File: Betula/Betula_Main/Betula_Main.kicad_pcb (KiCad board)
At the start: 2 copper layers, 39.4 x 110.1 mm, 172 parts, among them J1 Conn_02x15_Top_Bottom, J2 Conn_02x02_Top_Bottom, J3 Conn_02x15_Top_Bottom, J4 Conn_01x03_Male, J5 Conn_01x03_Male, J6 Conn_02x05_Odd_Even, Q1 FDS4435BZ, Q2 DMN3030LSS, U1 PCM1803A, U10 V1402, U11 74HCT125, U12 TLV9354, U13 TLV9354, U14 TLV9352, U15 TLV9354, U16 TLV9354, U2 PCM1803A, U3 PCM1803A, U4 PCM1803A, U5 LDK320A, U6 TL062, U7 PCM1681TPWPQ1, U8 74HC4050, U9 V1401

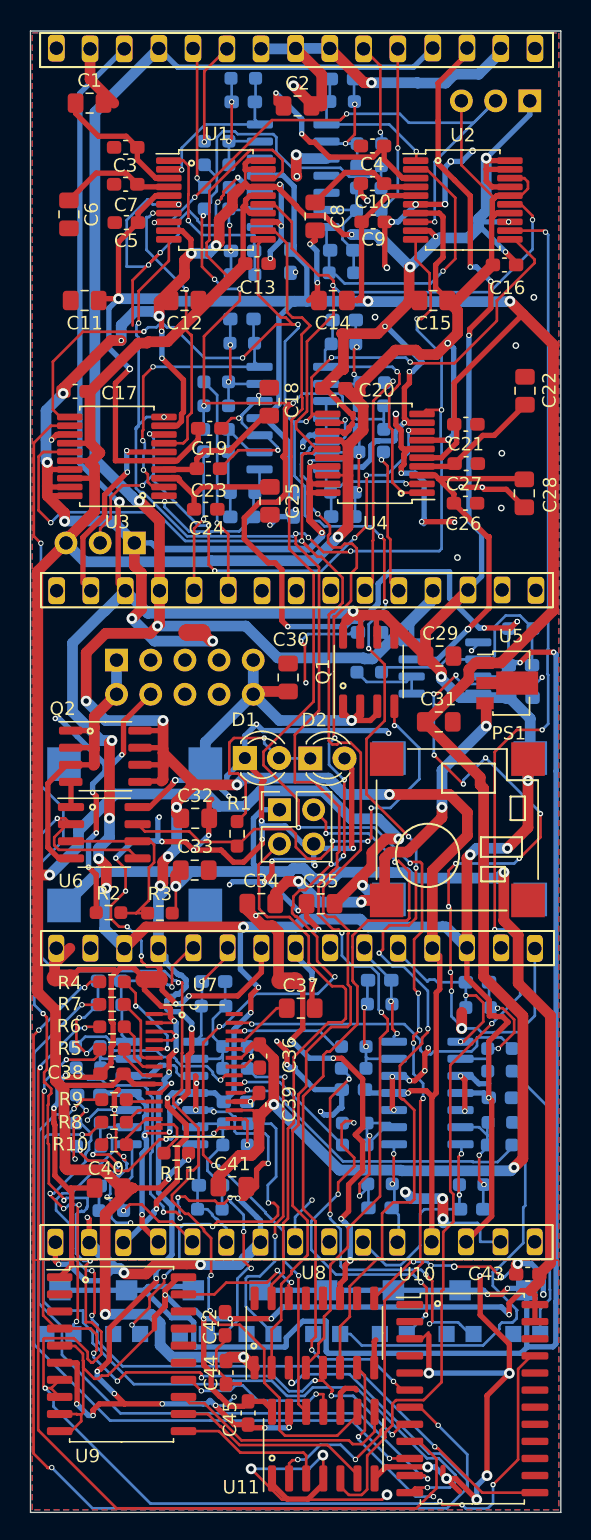
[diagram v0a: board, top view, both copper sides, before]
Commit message: Added Betula v1.5.1:  Improved noise floor, 4-layer main PCB, better Panel
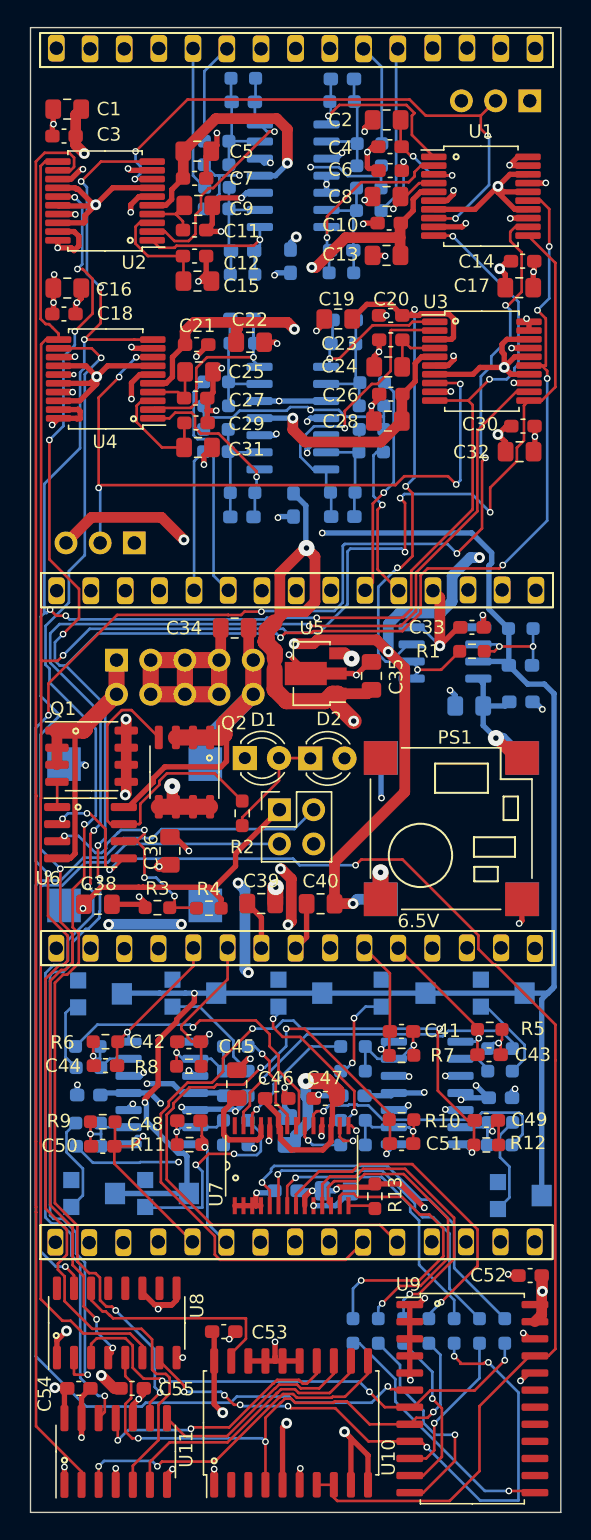
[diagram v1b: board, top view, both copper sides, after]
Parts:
- removed the C29 at (121.9, 78.6)
- removed NT1, NT2, NT3, NT4: NetTie_2, NetTie:NetTie-2_SMD_Pad2.0mm
- added C16: 10u, Capacitor_SMD:C_0805_2012Metric_Pad1.18x1.45mm_HandSolder, F.Cu at (94.2, 51.3)
- added C22: 10u, Capacitor_SMD:C_0805_2012Metric_Pad1.18x1.45mm_HandSolder, F.Cu at (107.8, 55.3)
- added C28: 10u, Capacitor_SMD:C_0805_2012Metric_Pad1.18x1.45mm_HandSolder, F.Cu at (118.0, 61.2)
- added C32: 10u, Capacitor_SMD:C_0805_2012Metric_Pad1.18x1.45mm_HandSolder, F.Cu at (127.8, 63.5)
- added C68: 10uF, Capacitor_SMD:C_0805_2012Metric_Pad1.18x1.45mm_HandSolder, B.Cu at (124.1, 82.3)
- C33: renamed from C56; moved to F.Cu
- C38: renamed from C33; value 10uF -> 22uF
- C39: renamed from C34; value 10uF -> 22uF
- C40: renamed from C35; value 10uF -> 22uF
- C41: renamed from C60; moved to F.Cu
- C42: renamed from C61; moved to F.Cu
- C43: renamed from C59; moved to F.Cu
- C44: renamed from C62; moved to F.Cu
- C48: renamed from C67; moved to F.Cu
- C49: renamed from C69; moved to F.Cu
- C50: renamed from C68; moved to F.Cu
- C51: renamed from C70; moved to F.Cu
- C73: renamed from C41; moved to B.Cu
- C74: renamed from C40; moved to B.Cu
- C75: renamed from C38; moved to B.Cu
- R1: renamed from R37; moved to F.Cu
- R10: renamed from R56; moved to F.Cu
- R11: renamed from R60; moved to F.Cu
- R12: renamed from R55; moved to F.Cu
- R5: renamed from R38; moved to F.Cu
- R55: renamed from R4; moved to B.Cu
- R56: renamed from R7; moved to B.Cu
- R57: renamed from R6; moved to B.Cu
- R58: renamed from R5; moved to B.Cu
- R59: renamed from R9; moved to B.Cu
- R6: renamed from R46; moved to F.Cu
- R60: renamed from R8; moved to B.Cu
- R61: renamed from R10; moved to B.Cu
- R7: renamed from R40; moved to F.Cu
- R8: renamed from R42; moved to F.Cu
- R9: renamed from R61; moved to F.Cu
- moved R55 39.0 mm to (126.7, 128.8), turned to 90 degrees
- moved R56 36.5 mm to (124.8, 128.8), turned to 90 degrees
- moved R57 34.0 mm to (123.0, 128.8), turned to 90 degrees
- moved R58 31.5 mm to (121.1, 128.8), turned to 90 degrees
- moved R59 27.5 mm to (119.2, 128.8), turned to 90 degrees
- moved R60 25.0 mm to (117.3, 128.8), turned to 90 degrees
- moved RV3 24.5 mm to (111.7, 103.7), turned to 0 degrees
- moved RV5 24.4 mm to (96.8, 103.7), turned to 0 degrees
- moved RV4 24.0 mm to (103.8, 103.7), turned to 0 degrees
- moved RV2 23.9 mm to (119.4, 103.7), turned to 0 degrees
- moved RV1 23.6 mm to (126.7, 103.7), turned to 0 degrees
- moved R61 22.5 mm to (115.4, 128.8), turned to 90 degrees
- moved C19 18.9 mm to (114.3, 53.6), turned to 180 degrees
- moved C3 17.2 mm to (94.0, 40.0), turned to 0 degrees
- moved C74 16.9 mm to (114.2, 118.4), turned to 0 degrees
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- renumbered C12 to C1, C9 to C10, C7 to C11, C3 to C12, C14 to C13, C16 to C14, C1 to C15, C15 to C17, C17 to C18, C28 to C19, C26 to C20, C19 to C21, C27 to C23, C22 to C24, C18 to C25, C21 to C26, C23 to C27, C24 to C29, C13 to C3, C20 to C30, C25 to C31, C30 to C34, C31 to C35, C32 to C36, C37 to C45, C36 to C46, C39 to C47, C11 to C5, C43 to C52, C42 to C53, C45 to C54, C44 to C55, C46 to C56, C47 to C57, C48 to C58, C50 to C59, C10 to C6, C49 to C60, C52 to C61, C51 to C62, C54 to C63, C53 to C64, C55 to C65, C57 to C66, C58 to C67, C64 to C69, C5 to C7, C65 to C70, C66 to C71, C63 to C72, C6 to C9, Q2 to Q1, Q1 to Q2, R11 to R13, R13 to R14, R12 to R15, R15 to R16, R14 to R18, R16 to R19, R1 to R2, R19 to R20, R20 to R21, R18 to R22, R21 to R23, R22 to R24, R23 to R25, R25 to R26, R24 to R28, R26 to R29, R2 to R3, R29 to R30, R32 to R31, R28 to R32, R31 to R33, R30 to R34, R33 to R35, R34 to R36, R35 to R37, R36 to R38, R3 to R4, R41 to R40, R43 to R41, R44 to R42, R47 to R43, R49 to R44, R52 to R45, R45 to R46, R48 to R47, R50 to R48, R51 to R49, R53 to R50, R54 to R51, R57 to R52, R58 to R53, R59 to R54, RV5 to RV4, RV6 to RV5, RV4 to RV6, U2 to U1, U9 to U10, U1 to U2, U4 to U3, U3 to U4, U10 to U9
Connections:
- C1 pad 2: GNDD -> GNDA
- C14 pad 1: GNDD -> GNDA
- C17 pad 2: GNDD -> GNDA
- C18 pad 1: GNDD -> GNDA
- C3 pad 1: GNDD -> GNDA
- C30 pad 1: GNDD -> GNDA
- C52 pad 1: GNDD -> GNDA
- C53 pad 1: GNDD -> GNDA
- C54 pad 1: GNDD -> GNDA
- C55 pad 1: GNDD -> GNDA
- C74 pad 2: GNDD -> GNDA
- C75 pad 1: GNDD -> GNDA
- J3 pad 16: GNDA -> unconnected-(J3-Pin_16-Pad16)
- J4 pad 1: GNDD -> GNDA
- J5 pad 1: GNDD -> GNDA
- PS3 pad 1: unconnected-(PS3-+VIN-Pad1) -> 12V_ IN
- U1 pad 13: GNDD -> GNDA
- U1 pad 17: GNDD -> GNDA
- U1 pad 19: GNDD -> GNDA
- U1 pad 20: GNDD -> GNDA
- U1 pad 9: GNDD -> GNDA
- U10 pad 1: GNDD -> GNDA
- U10 pad 15: GNDD -> GNDA
- U10 pad 16: GNDD -> GNDA
- U10 pad 17: GNDD -> GNDA
- U10 pad 18: GNDD -> GNDA
- U10 pad 6: GNDD -> GNDA
- U11 pad 1: GNDD -> GNDA
- U11 pad 10: GNDD -> GNDA
- U11 pad 13: GNDD -> GNDA
- U11 pad 4: GNDD -> GNDA
- U11 pad 7: GNDD -> GNDA
- U2 pad 13: GNDD -> GNDA
- U2 pad 17: GNDD -> GNDA
- U2 pad 19: GNDD -> GNDA
- U2 pad 20: GNDD -> GNDA
- U2 pad 9: GNDD -> GNDA
- U3 pad 13: GNDD -> GNDA
- U3 pad 17: GNDD -> GNDA
- U3 pad 19: GNDD -> GNDA
- U3 pad 20: GNDD -> GNDA
- U3 pad 9: GNDD -> GNDA
- U4 pad 13: GNDD -> GNDA
- U4 pad 17: GNDD -> GNDA
- U4 pad 19: GNDD -> GNDA
- U4 pad 20: GNDD -> GNDA
- U4 pad 9: GNDD -> GNDA
- U7 pad 1: GNDD -> GNDA
- U7 pad 10: GNDD -> GNDA
- U7 pad 2: GNDD -> GNDA
- U7 pad 3: GNDD -> GNDA
- U7 pad 4: GNDD -> GNDA
- U8 pad 11: GNDD -> GNDA
- U8 pad 8: GNDD -> GNDA
- U8 pad 9: GNDD -> GNDA
- U9 pad 1: GNDD -> GNDA
- U9 pad 2: GNDD -> GNDA
- U9 pad 20: GNDD -> GNDA
- U9 pad 22: GNDD -> GNDA
- U9 pad 3: GNDD -> GNDA
- U9 pad 4: GNDD -> GNDA
- U9 pad 5: GNDD -> GNDA
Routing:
- net GNDD: track 432.3 -> 0.00 mm, vias 63 -> 0
- net GNDA: track 462.8 -> 219.6 mm, vias 115 -> 96
- net SCLK_5V: track 99.0 -> 37.7 mm, vias 5 -> 3
- net DIN1/2: track 59.5 -> 11.4 mm, vias 2 -> 1
- net -REF: track 236.4 -> 190.2 mm, vias 13 -> 6
- net OUT6: track 16.8 -> 60.4 mm, vias 2 -> 3
- net DIN3/4: track 55.5 -> 12.6 mm, vias 2 -> 1
- net DIN5/6: track 58.8 -> 16.3 mm, vias 2 -> 1
- net OUT5: track 8.35 -> 50.7 mm, vias 2 -> 3
- net DIN7/8: track 57.1 -> 19.1 mm, vias 4 -> 1
- net BCLK_5V: track 83.4 -> 46.5 mm, vias 4 -> 7
- net Net-(R46-Pad2): track 36.2 -> 4.99 mm, vias 6 -> 0
- net ADAT_RX: track 59.7 -> 88.4 mm, vias 4 -> 1
- net WCLK_3.3V: track 145.5 -> 171.8 mm, vias 9 -> 11
- net DOUT3/4: track 109.6 -> 135.7 mm, vias 4 -> 6
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- added copper zone on In1.Cu, net GNDA
- removed copper zone on B.Cu, net GNDA
- removed copper zone on F.Cu, net GNDA
- removed copper zone on B.Cu, net GNDD
- removed copper zone on F.Cu, net GNDD
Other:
- board size 39.4 x 110.1 mm -> 39.4 x 110.3 mm
- copper layers 2 -> 4
- board text added: "3.3V"
- board text added: "5V"
- board text added: "6.5V"
- board text added: "Blattwerk Betula v1.5.1 CC BY-NC-SA 4.0"
- board text removed: "Blattwerk Betula v1.4.1 CC BY-NC_SA 4.0"

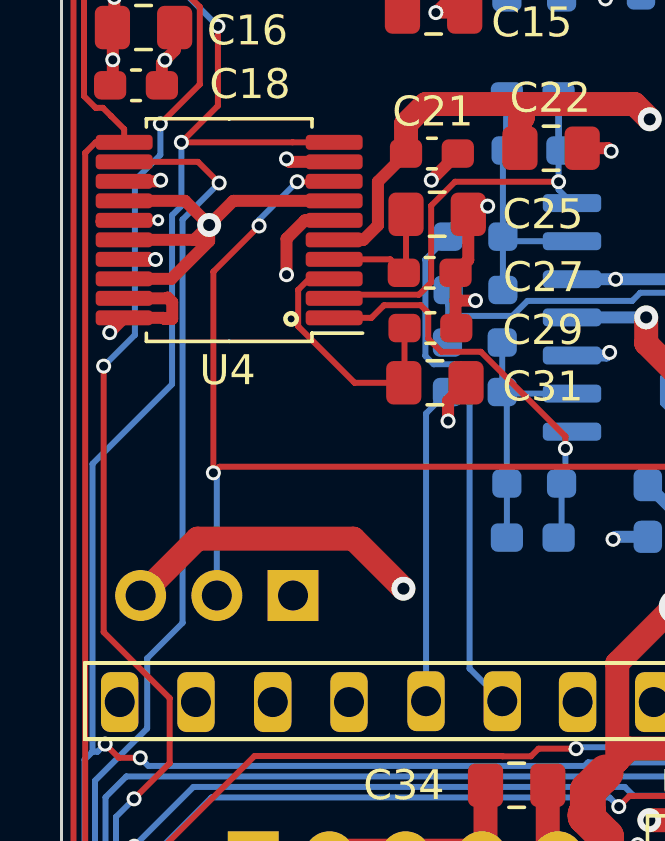
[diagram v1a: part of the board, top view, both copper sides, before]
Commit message: fixed 2mm via to 3mm in order to avoid extra cost in manufacturing
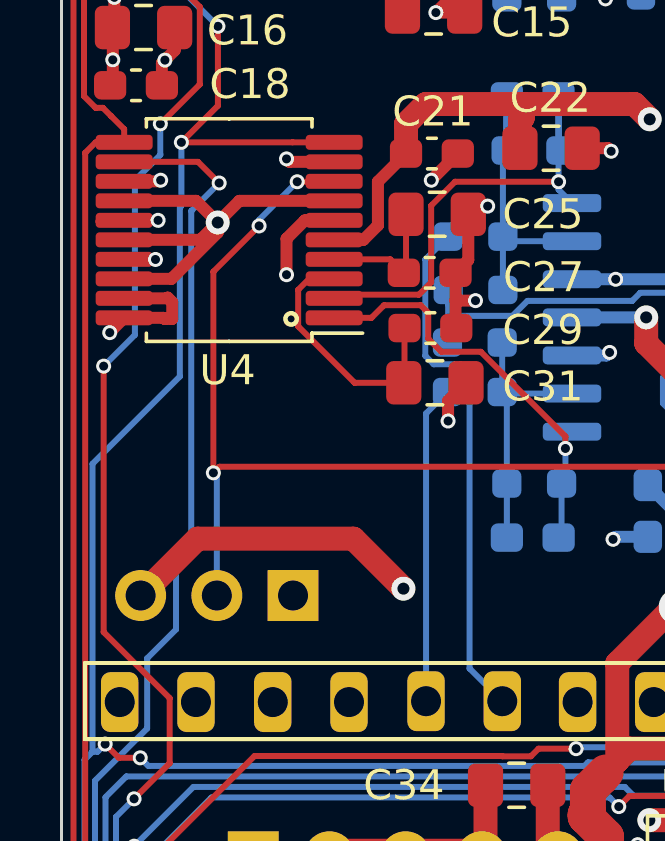
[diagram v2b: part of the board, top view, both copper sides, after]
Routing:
- net +3.3V: track 317.4 -> 318.1 mm

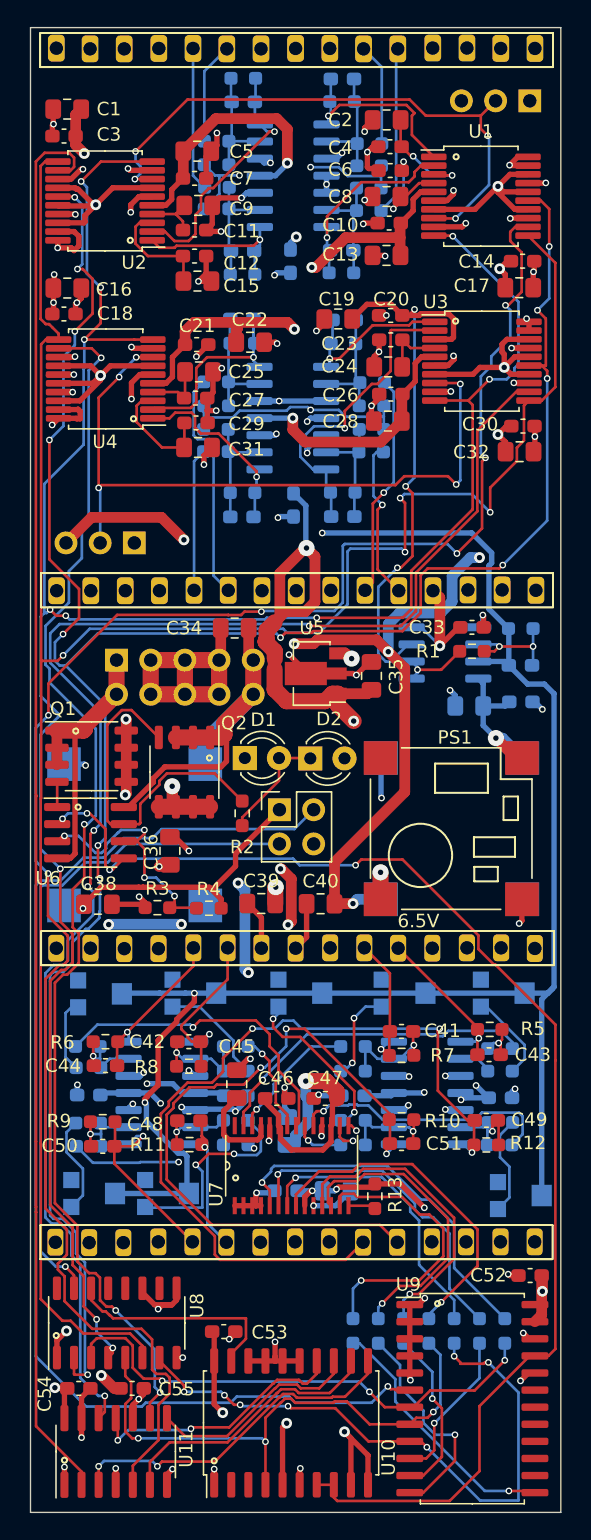
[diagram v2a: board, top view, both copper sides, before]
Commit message: Changed DC/DC converters to R-78Kx, updated to v1.5.2
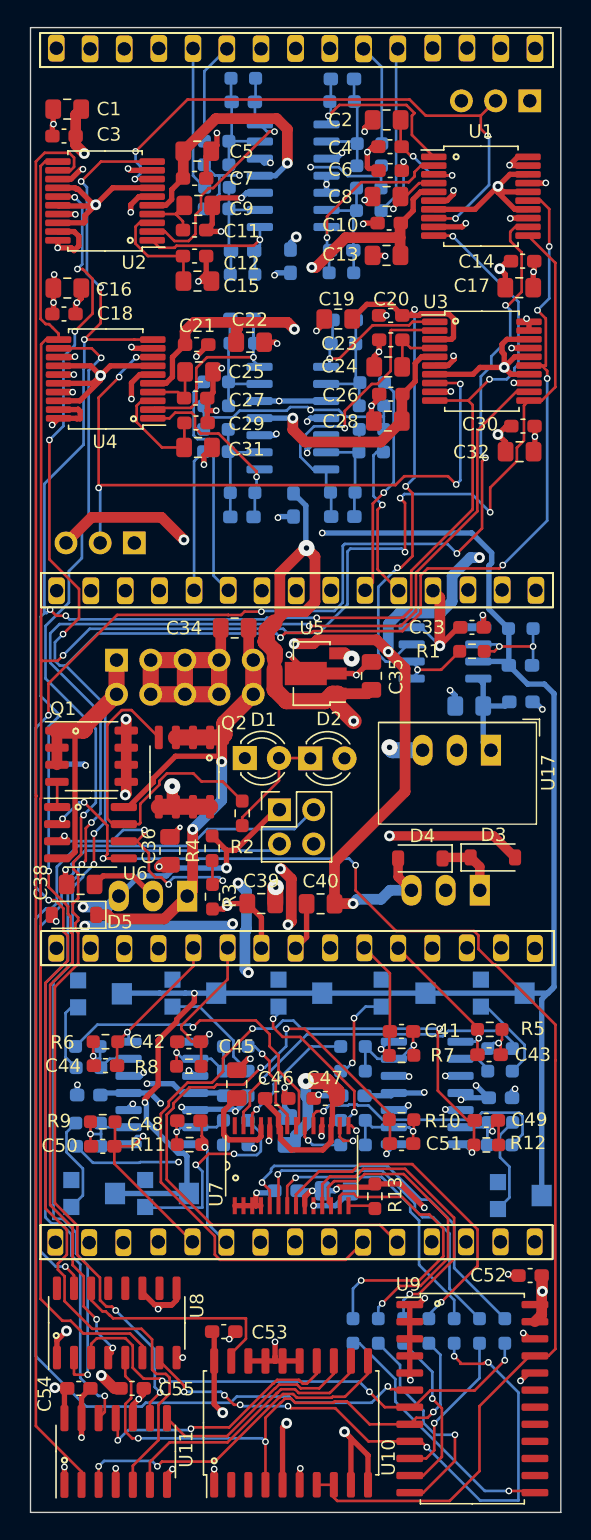
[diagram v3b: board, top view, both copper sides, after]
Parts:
- removed PS1: PXO7806-500-M-TR, Eigenes:CONV_PXO7803-500-M-TR
- removed PS2: PXO7803-500-M-TR, Eigenes:CONV_PXO7803-500-M-TR
- removed PS3: PXO7805-500-M-TR, Eigenes:CONV_PXO7803-500-M-TR
- added D3: 1N5819, Diode_SMD:D_SOD-123, F.Cu at (125.8, 93.6)
- added D4: 1N5819, Diode_SMD:D_SOD-123, F.Cu at (120.4, 93.7)
- added D5: 1N5819, Diode_SMD:D_SOD-123, F.Cu at (94.7, 97.9)
- added U17: R-78K6.5-0.5, Eigenes:Converter_DCDC_RECOM_R-78K, F.Cu at (125.7, 85.6)
- added U18: R-78K5-0.5, Eigenes:Converter_DCDC_RECOM_R-78K, B.Cu at (103.1, 96.5)
- added U19: R-78K3.3-0.5, Eigenes:Converter_DCDC_RECOM_R-78K, B.Cu at (124.9, 96.0)
- moved R4 4.46 mm to (105.0, 92.9), turned to 90 degrees
- moved R3 4.17 mm to (105.0, 96.5), turned to 90 degrees
- moved C38 1.96 mm to (95.2, 95.6)
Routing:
- net -12V: track 229.2 -> 257.2 mm
- net 12V_ IN: track 31.3 -> 42.6 mm, vias 0 -> 2
- net Net-(D3-A): track 32.4 -> 42.0 mm, vias 3 -> 4
- net +3.3V: track 318.1 -> 323.2 mm
- net +5V: track 132.8 -> 136.4 mm, vias 6 -> 9
- net +12V: track 256.1 -> 258.7 mm, vias 5 -> 4
- net Net-(U6A-+): track 18.8 -> 20.7 mm
- net ERROR: track 98.9 -> 100.0 mm
- net GNDA: track 219.6 -> 218.7 mm, vias 96 -> 94
- net SCLK_3.3V: track 174.7 -> 173.8 mm
- net WCLK_3.3V: track 171.8 -> 171.1 mm
- net DOUT7/8: track 113.3 -> 112.7 mm
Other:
- board text added: "Blattwerk Betula v1.5.2 CC BY-NC-SA 4.0"
- board text removed: "3.3V"
- board text removed: "5V"
- board text removed: "6.5V"
- board text removed: "Blattwerk Betula v1.5.1 CC BY-NC-SA 4.0"
